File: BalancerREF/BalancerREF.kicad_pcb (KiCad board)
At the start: 4 copper layers, 50 x 50 mm, 81 parts, among them J1 USB4105-GF-A, J2 LiPo 500mAh PROTECTED, J3 MAG+ / MAG- PTH, J4 GPS MODULE 3V3 UART, J5 OPTICAL HEAD 7-WAY, Q4 AO3401A, SW1 POWER, SW2 ACQUIRE, SW3 BOOT / SERVICE, U1 ESP32-S3-MINI-1-N8, U10 SN74LVC1G123DCTR, U2 IIS3DWBTR, U3 LM1815MX/NOPB, U5 BQ24075RGT, U6 TPS63031DSKR, U7 SRV05-4MR6T1G, U9 SN74LVC1G132DBVR

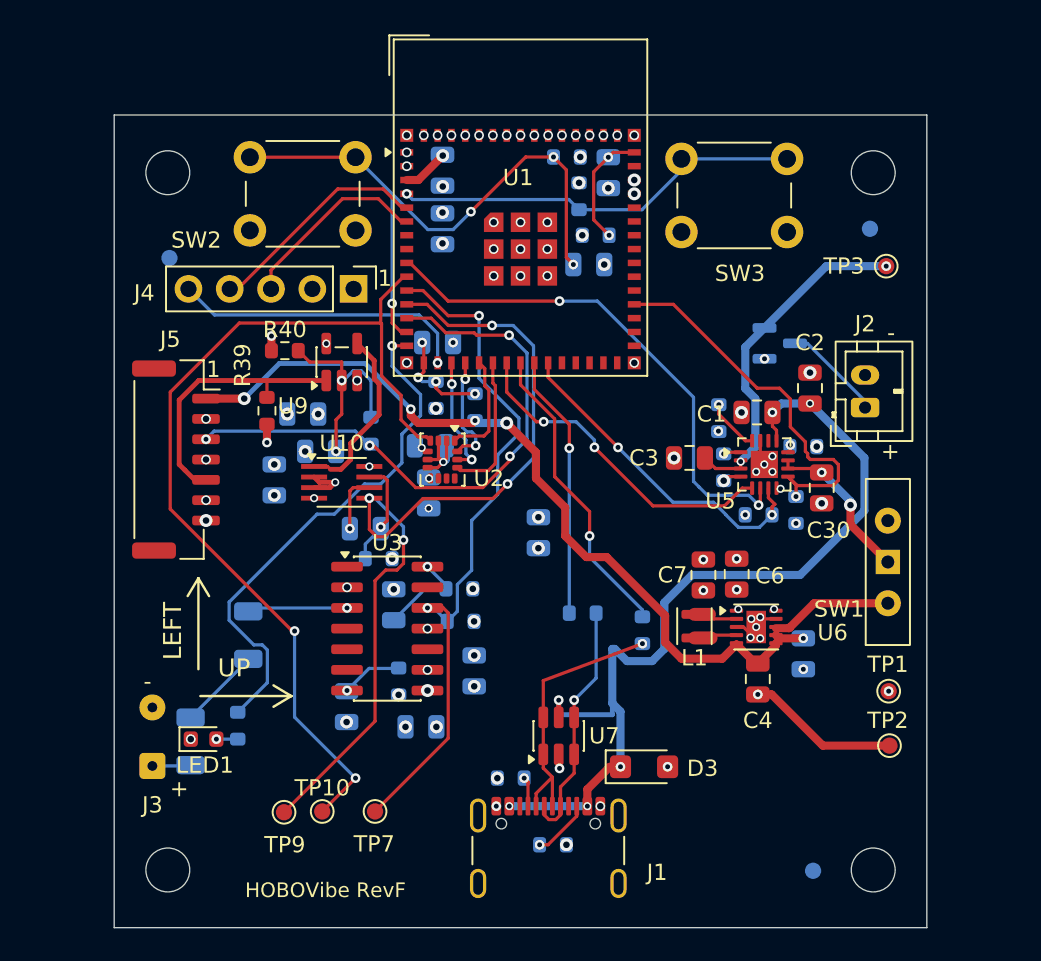
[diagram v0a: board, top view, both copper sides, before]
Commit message: feat: hand re-layout of the USB front end
U7 moved to (131.20, 136.75) rot -90, R39 to (111.40, 114.60) and R40 to
(109.65, 114.60), with the data pair re-routed to suit. R6 and R7 stay put.

D3's corrected polarity and U7's IO3/IO4 wiring both carry over unchanged,
so each USB line still enters one pad of the array and leaves the pad
opposite rather than spurring off the series resistors.

kicad_pro: sch_revision F -> G, sheet_component_classes enabled.

DRC 7 violations, 0 unconnected. The seven are the pre-existing footprint
issues - the GCT USB-C peg-to-pad spacing (x4), the ESP32 antenna overhang
(x2) and the local U1 footprint edit. Schematic parity is 7, all of them
extra_footprint on the mounting holes and fiducials, which have no symbols.
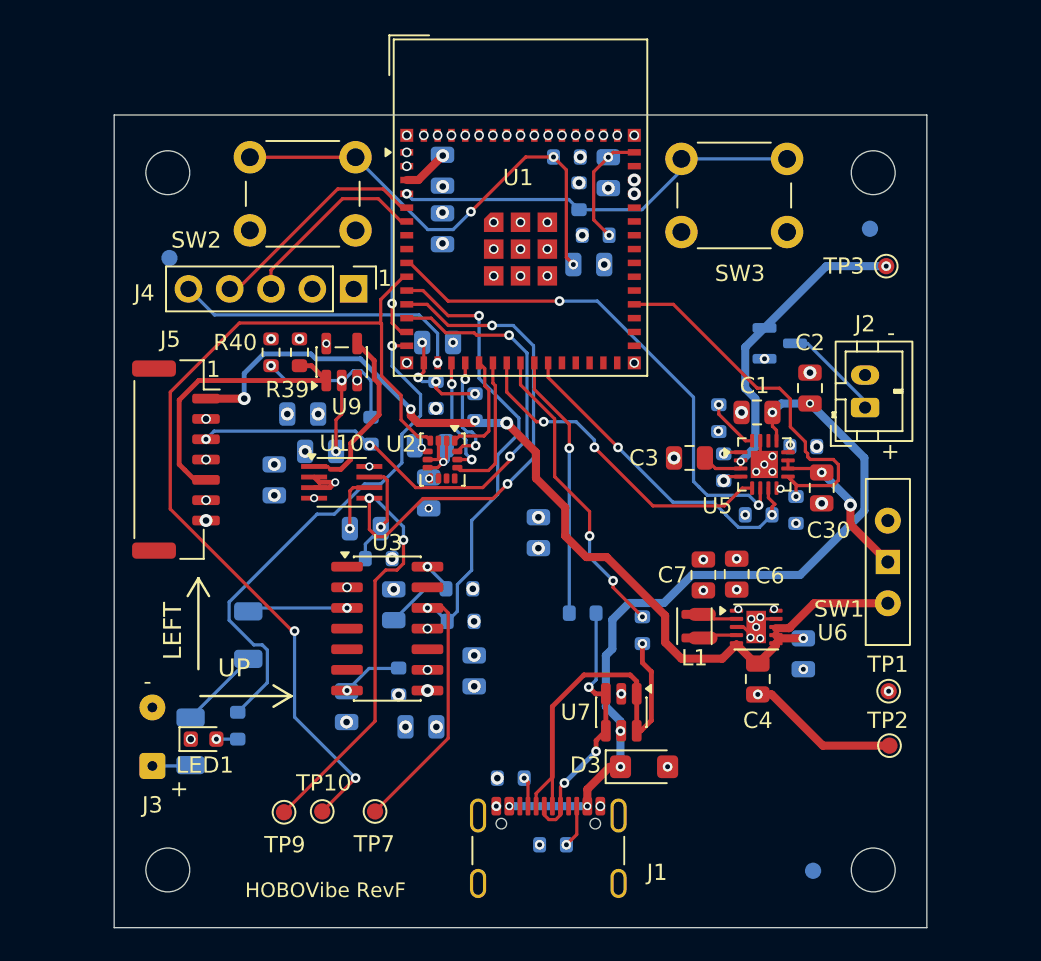
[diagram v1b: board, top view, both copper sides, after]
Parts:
- R35, R36, R37, R38: footprint R_0603_1608Metric -> Resistor_SMD:R_0603_1608Metric
- U5: footprint QFN-16-1EP_3x3mm_P0.5mm_EP1.675x1.675mm -> Package_DFN_QFN:QFN-16-1EP_3x3mm_P0.5mm_EP1.675x1.675mm
- moved R39 4.12 mm to (111.4, 114.6), turned to 90 degrees
- moved U7 4.11 mm to (131.2, 136.8), turned to -90 degrees
- moved R40 0.86 mm to (109.7, 114.6), turned to 90 degrees
- turned R2 to 0 degrees
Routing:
- net /USB_CONN_D-: track 16.7 -> 23.6 mm
- net /USB_VBUS: track 55.6 -> 48.7 mm
- net GND: track 23.4 -> 20.5 mm
- net /SYS_SW: track 57.5 -> 58.9 mm
- net /USB_CONN_D+: track 15.1 -> 16.3 mm, vias 1 -> 3
- net /OPT_COMP: track 16.6 -> 17.6 mm
- net Net-(J1-CC2): track 3.62 -> 2.64 mm
- net Net-(C26-Pad1): track 13.2 -> 13.8 mm, vias 2 -> 3
- net Net-(U1-USB_D-): track 18.8 -> 18.7 mm, vias 1 -> 3

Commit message: feat: BalancerCarrier on a FeatherS3[D], and two board fixes
Adds BalancerCarrier: the HOBOVibe instrument rebuilt as a carrier around an
Unexpected Maker FeatherS3[D] (ESP32-S3, 16 MB flash, 8 MB QSPI PSRAM), so the
MCU, LiPo charger, fuel gauge and USB come from a proven module instead of being
respun. 31 parts, ERC 0 violations.

The module is a Feather, so U1 uses Module:Adafruit_Feather-compatible geometry -
Unexpected Maker's own 28-pad footprint and symbol, checked pin-for-pin against
their FeatherS3[D] schematic headers J1 and JP3. That makes the footprint
vendor-independent: another Feather drops in without a respin, which is the
exposure that bit this project when the DFR0975 went pre-order only.

Seven parts came out once the module's own hardware was traced properly. LDO2
(NCP167BMX330TBG, 700 mA) is fed from VBUS, which ORs USB and VBAT, so it is live
on battery and powers the GPS - the discrete load switch went. The onboard
MAX17048 fuel gauge reads the cell directly over I2C, so the supply-sense divider
went with it.

Board fixes, both found by diffing against BalancerREF rather than trusting what
was drawn:

  BalancerREF  R30/C28 100k/1n -> 10k/10n. TI SCES586E section 5.8 characterises
               10k/10n at tw 100-110 us across all four supply voltages; 100k is
               ten times beyond the largest Rext TI characterises.

  OptHead      PD1 BPW34S -> SFH 2440. The old line was unbuildable: an SMD
               footprint against Vishay's BPW34S, which doc 81521 calls "leaded",
               naming an Osram part that is out of production. SFH 2440 is
               pad-identical, peaks at 620 nm against the 625 nm emitter, and
               blocks the IR the BPW34 was most sensitive to. C21 10 pF -> 22 pF:
               junction capacitance roughly doubles, so Cf_min rises to ~12.3 pF
               and the fitted 10 pF would peak. NOT SFH 2430 - 200 us rise time.

PhotoTach-BOM.csv rebuilt. It had nine classes of error, the worst struc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
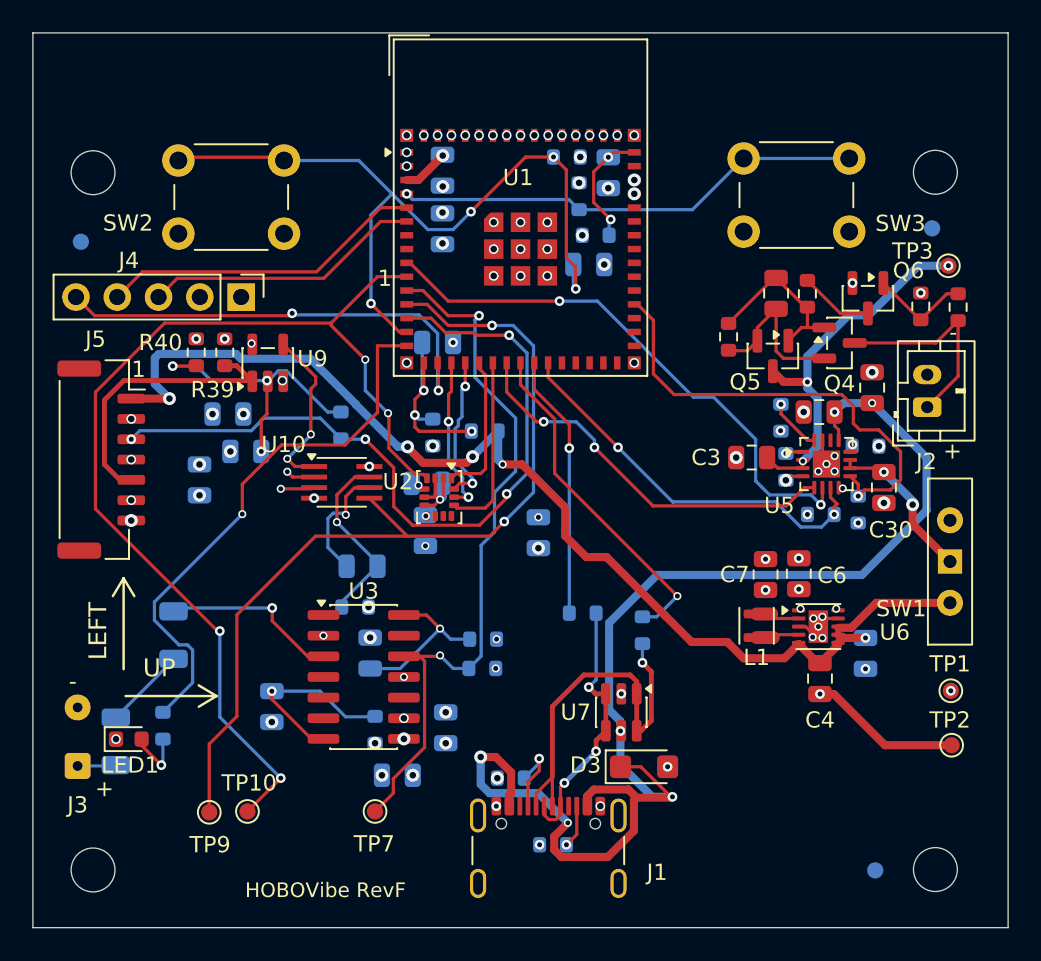
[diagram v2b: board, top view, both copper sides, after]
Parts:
- added C31: 10n, Capacitor_SMD:C_0805_2012Metric, F.Cu at (140.7, 111.0)
- added Q5: AO3401A, Package_TO_SOT_SMD:SOT-23, F.Cu at (140.5, 114.8)
- added Q6: AO3400A, Package_TO_SOT_SMD:SOT-23, F.Cu at (146.4, 111.3)
- added R41: 1M, Resistor_SMD:R_0603_1608Metric, F.Cu at (137.8, 113.7)
- added R42: 100k, Resistor_SMD:R_0603_1608Metric, F.Cu at (142.7, 111.0)
- added R43: 100k, Resistor_SMD:R_0603_1608Metric, F.Cu at (151.9, 111.8)
- added R44: 1M, Resistor_SMD:R_0603_1608Metric, F.Cu at (149.6, 111.8)
- C28: value 1n C0G -> 10n C0G
- Q4: moved to F.Cu
- R30: value 100k -> 10k
- moved J4 6.94 mm to (107.8, 111.2)
- moved FID5 5.54 mm to (98.0, 107.8)
- moved C26 4.60 mm to (108.1, 120.7)
- moved R13 4.60 mm to (100.1, 138.5)
- moved R39 4.60 mm to (106.8, 114.6)
- moved R40 4.60 mm to (105.0, 114.6)
- moved TP9 4.60 mm to (105.8, 142.9)
- moved C19 4.60 mm to (109.7, 136.4)
- moved C27 4.60 mm to (107.0, 118.4)
- moved C29 4.60 mm to (105.2, 122.5)
- moved H1 4.60 mm to (98.7, 146.4)
- moved H3 4.60 mm to (98.7, 103.5)
- moved J3 4.60 mm to (97.8, 140.1)
- moved J5 4.60 mm to (99.2, 121.2)
- moved LED1 4.60 mm to (100.9, 138.4)
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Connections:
- Q4 pad 1: GND -> /BPS_GATE
- Q4 pad 2: /BAT -> /BPS_SRC
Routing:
- net /USB_VBUS: track 48.7 -> 80.3 mm
- net /SYS_SW: track 58.9 -> 69.6 mm
- net /BPS_GATE: track 0.00 -> 10.6 mm
- net /GPS_PPS: track 18.3 -> 28.6 mm, vias 1 -> 2
- net /BPS_SRC: track 0.00 -> 10.2 mm
- net /OPT_LED_EN: track 36.1 -> 46.2 mm
- net /ACQUIRE_BUTTON: track 38.6 -> 47.1 mm
- net Net-(U3-PEAK_DET): track 3.75 -> 11.9 mm
- net Net-(J2-Pin_1): track 6.18 -> 13.4 mm
- net /ACCEL_DRDY: track 58.6 -> 65.8 mm, vias 2 -> 4
- net Net-(Q6-G): track 0.00 -> 6.20 mm
- net /GPS_UART_TX: track 13.9 -> 20.1 mm
- net /SUPPLY_SENSE: track 6.48 -> 12.0 mm, vias 4 -> 3
- net /GPS_UART_RX: track 11.9 -> 17.2 mm
- net /CHG_STAT: track 24.0 -> 28.9 mm
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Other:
- board size 50 x 50 mm -> 60 x 55 mm
